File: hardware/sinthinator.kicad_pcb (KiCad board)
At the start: 2 copper layers, 100.9 x 121.4 mm, 39 parts, among them J1 3.5mm TRRS, J2 USB_C_Receptacle, SW1 SW_Push, SW2 SW_Push, SW3 SW_Push, U1 CAP1206-x-SL, U2 STM32C011J4Mx, U3 MCP4725xxx-xCH, U4 CAP1206-x-SL, U5 CAP1206-x-SL, U7 AMS1117-3.3, U8 PAM8302AAD

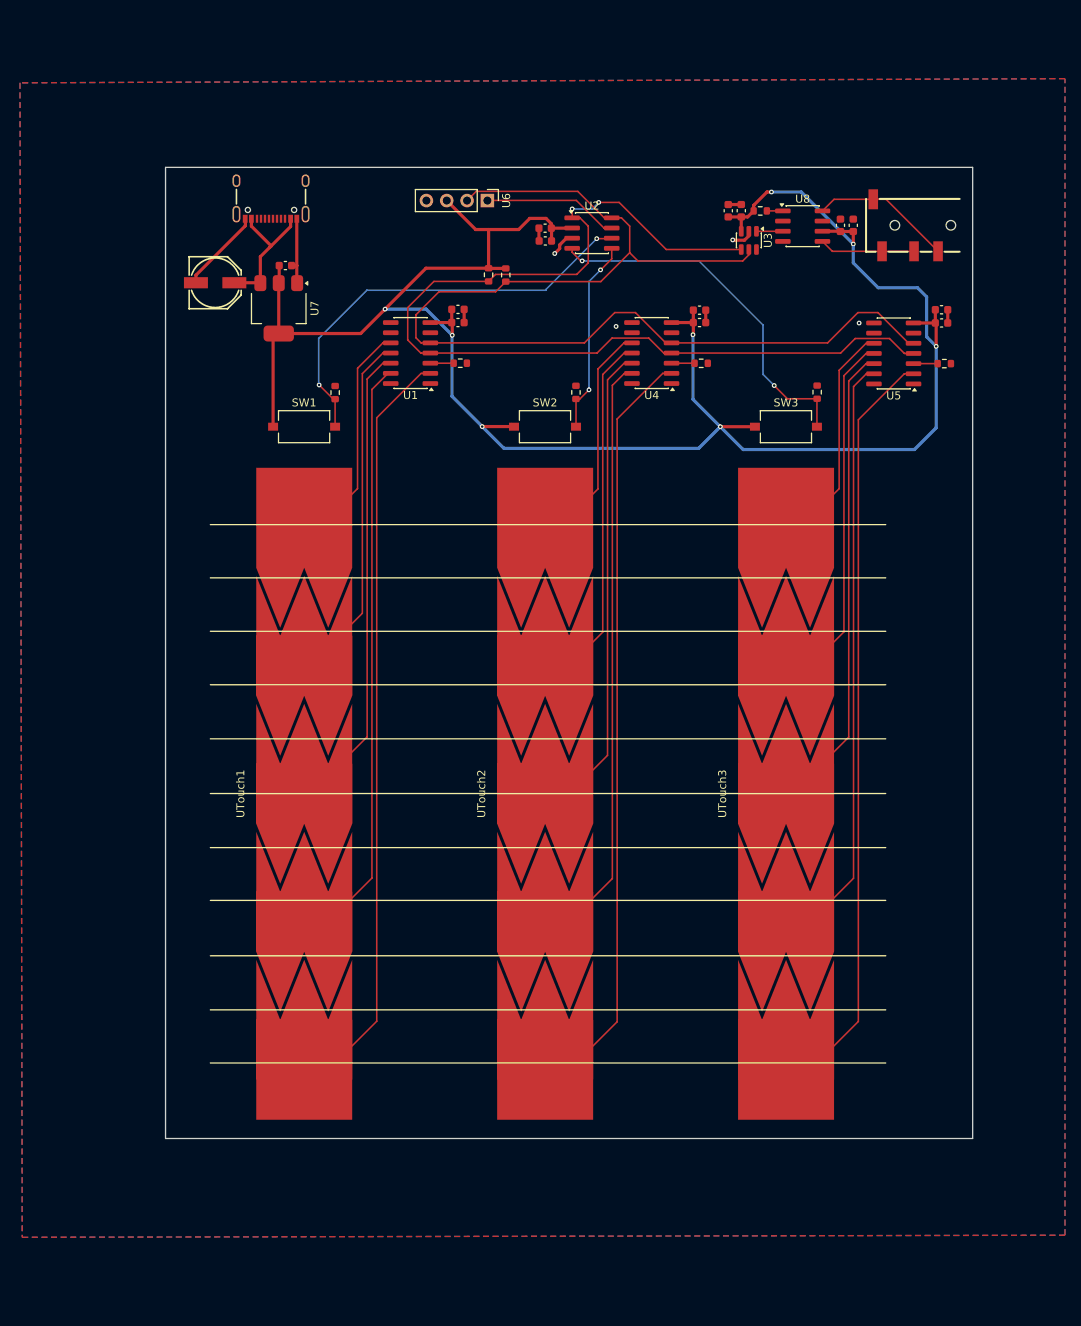
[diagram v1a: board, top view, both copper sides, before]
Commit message: Add the usb CC resistors + reduce some wasted space on board
Also added mounting holes in the same commit but don't tell anyone
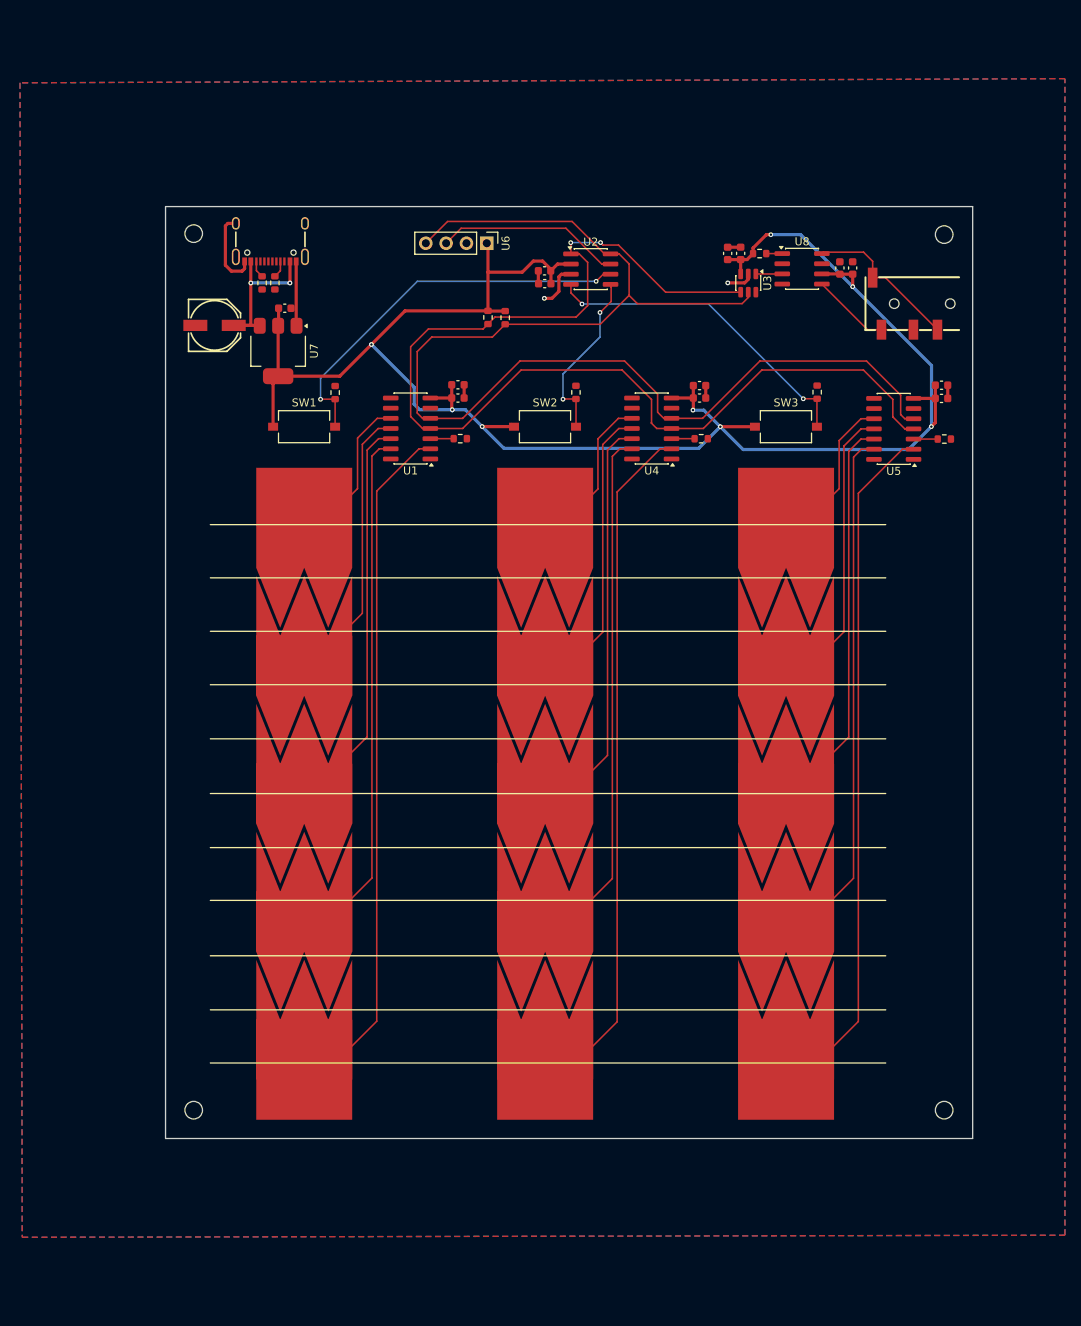
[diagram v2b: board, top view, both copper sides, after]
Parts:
- added R10: 5.1k, PCM_SparkFun-Resistor:R_0603_1608Metric, F.Cu at (113.8, 46.0)
- added R11: 5.1k, PCM_SparkFun-Resistor:R_0603_1608Metric, F.Cu at (112.2, 46.0)
- added REF**: MountingHole_2.2mm_M2, MountingHole:MountingHole_2.2mm_M2, F.Cu at (197.4, 40.0)
- added REF**: MountingHole_2.2mm_M2, MountingHole:MountingHole_2.2mm_M2, F.Cu at (103.6, 149.4)
- added REF**: MountingHole_2.2mm_M2, MountingHole:MountingHole_2.2mm_M2, F.Cu at (103.6, 39.9)
- added REF**: MountingHole_2.2mm_M2, MountingHole:MountingHole_2.2mm_M2, F.Cu at (197.4, 149.4)
- moved J1 9.79 mm to (194.7, 48.6)
- moved R8 9.43 mm to (167.1, 65.5)
- moved U1 9.43 mm to (130.7, 64.2)
- moved U4 9.43 mm to (160.9, 64.2)
- moved C10 9.43 mm to (136.7, 60.4)
- moved C11 9.43 mm to (166.9, 58.9)
- moved C12 9.43 mm to (166.9, 60.4)
- moved C13 9.43 mm to (197.1, 60.5)
- moved C14 9.43 mm to (197.1, 58.8)
- moved C9 9.43 mm to (136.7, 58.8)
- moved R7 9.43 mm to (136.9, 65.5)
- moved R9 9.43 mm to (197.4, 65.5)
- moved U5 9.43 mm to (191.1, 64.3)
- moved C1 5.33 mm to (147.5, 46.1)
- moved C2 5.33 mm to (147.5, 44.5)
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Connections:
- J2 pad A5: unconnected-(J2-CC1-PadA5) -> Net-(J2-CC1)
- J2 pad B5: unconnected-(J2-CC2-PadB5) -> Net-(J2-CC2)
- U6 pad 1: Net-(U2-PA13) -> 3.3V
- U6 pad 2: Net-(U1-SMCLK) -> GND
- U6 pad 3: 3.3V -> Net-(U2-PA13)
- U6 pad 4: GND -> Net-(U1-SMCLK)
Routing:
- net 3.3V: track 260.0 -> 232.4 mm
- net Net-(U1-SMCLK): track 143.8 -> 163.6 mm
- net Net-(U1-SMDATA): track 128.2 -> 145.0 mm
- net Net-(U5-CS1): track 93.0 -> 83.7 mm
- net Net-(U1-CS1): track 93.0 -> 83.7 mm
- net Net-(U4-CS1): track 93.0 -> 83.7 mm
- net Net-(U1-CS3): track 53.3 -> 44.1 mm
- net Net-(U4-CS2): track 72.4 -> 63.3 mm
- net Net-(U1-CS4): track 38.5 -> 29.4 mm
- net Net-(U5-CS2): track 72.4 -> 63.3 mm
- net Net-(U5-CS4): track 42.9 -> 33.9 mm
- net Net-(U5-CS5): track 25.7 -> 16.6 mm
- net Net-(U5-CS3): track 53.3 -> 44.2 mm
- net Net-(U4-CS3): track 57.6 -> 48.6 mm
- net Net-(U4-CS4): track 42.9 -> 33.9 mm
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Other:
- board size 100.9 x 121.4 mm -> 100.9 x 116.5 mm

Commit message: Update caps on power regulator
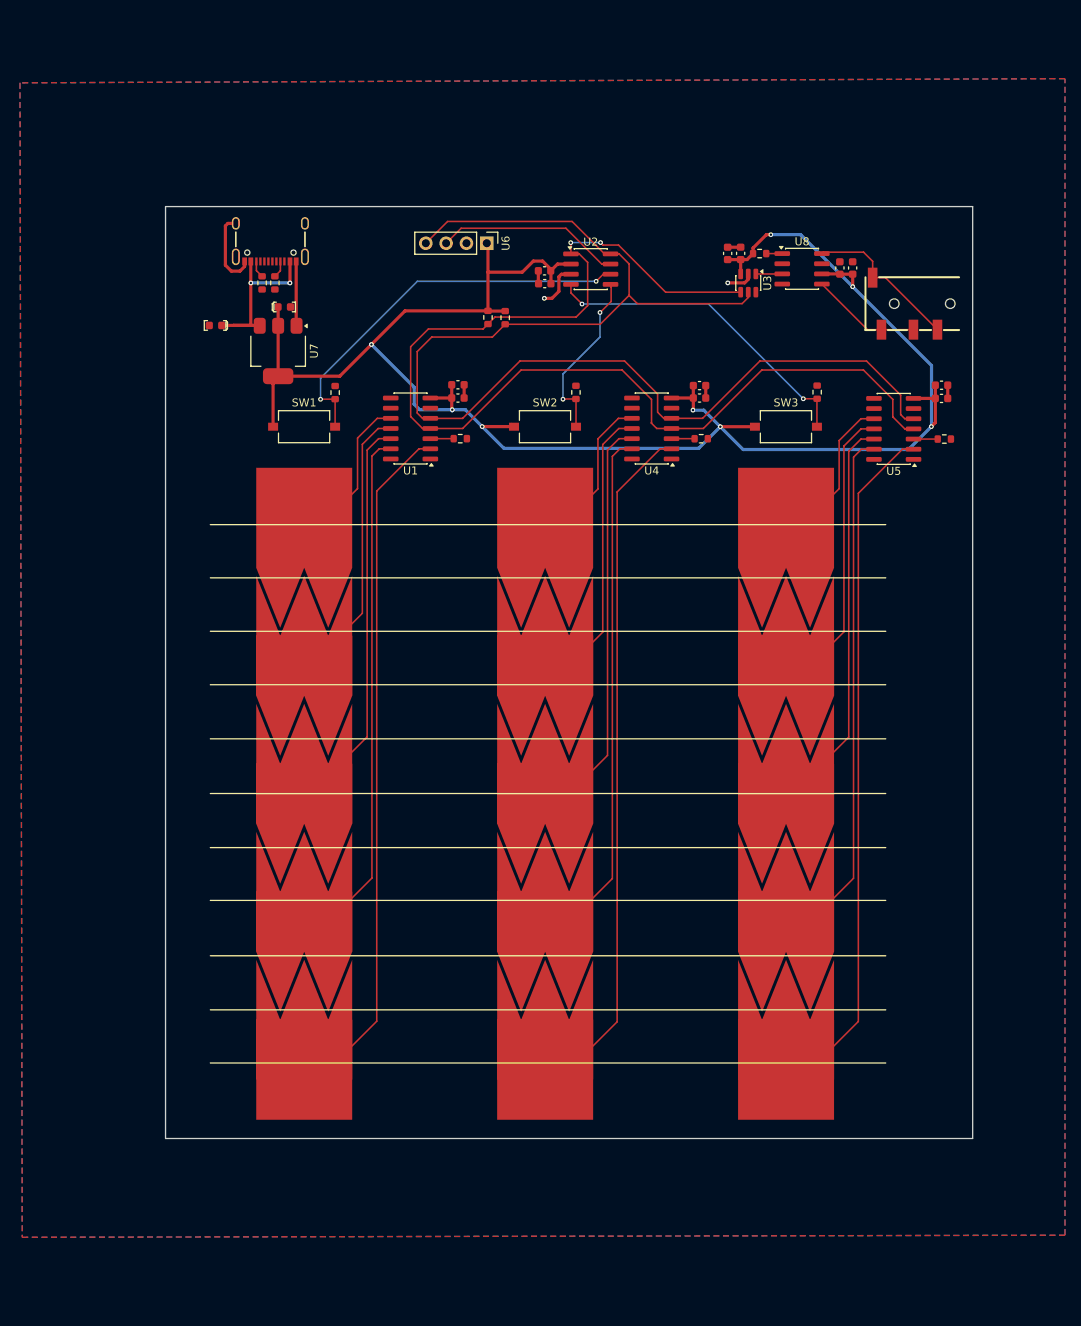
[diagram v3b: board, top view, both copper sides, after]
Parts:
- removed REF** (x4): MountingHole_2.2mm_M2, MountingHole:MountingHole_2.2mm_M2
- C3: value 22uF -> 10uF; footprint PCM_SparkFun-Capacitor:C_0603_1608Metric -> PCM_SparkFun-Capacitor:C_0603_1608Metric_Polar
- C4: value 100uF -> 10uF; footprint PCM_SparkFun-Capacitor:Panasonic_D -> PCM_SparkFun-Capacitor:C_0603_1608Metric_Polar
- moved C4 9.02 mm to (114.9, 49.0)
- moved C3 8.92 mm to (106.3, 51.4), turned to 180 degrees
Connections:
- C3 pad 1: 3.3V -> /+5V
- C4 pad 1: /+5V -> 3.3V
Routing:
- net /+5V: track 21.0 -> 22.5 mm

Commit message: Clean up + silkscreen bits
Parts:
- added M2: MountingHole_2.2mm_M2, MountingHole:MountingHole_2.2mm_M2, F.Cu at (103.8, 154.6)
- added M2: MountingHole_2.2mm_M2, MountingHole:MountingHole_2.2mm_M2, F.Cu at (197.4, 154.6)
- added M2: MountingHole_2.2mm_M2, MountingHole:MountingHole_2.2mm_M2, F.Cu at (197.4, 45.4)
- added M2: MountingHole_2.2mm_M2, MountingHole:MountingHole_2.2mm_M2, F.Cu at (103.8, 45.4)
- J2: value USB_C_Receptacle -> USB-C
- U1, U4, U5: value CAP1206-x-SL -> CAP1206
- U3: value MCP4725xxx-xCH -> MCP4725
- U8: value PAM8302AAD -> PAM8302A
- moved R5 5.24 mm to (181.6, 64.9)
- moved R9 5.24 mm to (197.4, 70.8)
- moved C11 5.24 mm to (166.9, 64.1)
- moved C14 5.24 mm to (197.1, 64.1)
- moved C3 5.24 mm to (106.3, 56.6)
- moved C4 5.24 mm to (114.9, 54.3)
- moved C5 5.24 mm to (184.4, 49.4)
- moved C6 5.24 mm to (186.0, 49.4)
- moved C7 5.24 mm to (170.4, 47.6)
- moved C8 5.24 mm to (172.0, 47.6)
- moved C9 5.24 mm to (136.7, 64.0)
- moved J1 5.24 mm to (194.7, 53.9)
- moved J2 5.24 mm to (113.2, 48.9)
- moved R1 5.24 mm to (142.6, 55.6)
- moved R10 5.24 mm to (113.8, 51.3)
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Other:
- board text added: "sinthinator v1"
- board text added: "♫"

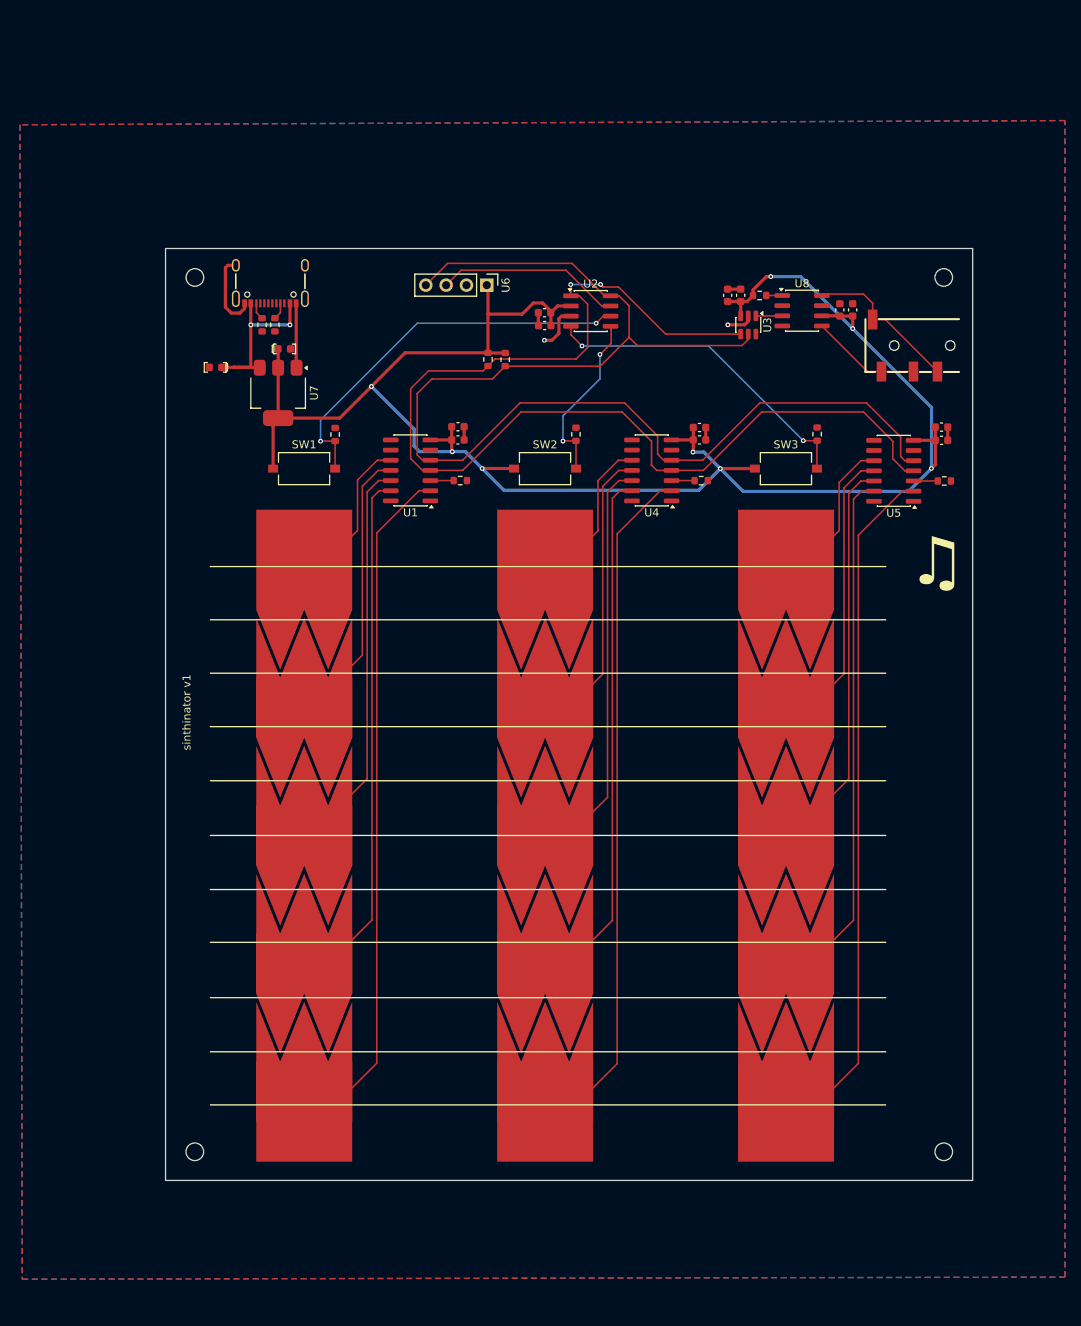
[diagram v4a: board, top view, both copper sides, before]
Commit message: Switch to STM32C011F6 for mcu to get more pins
+ add NRST header + i2s as header pins for debugging
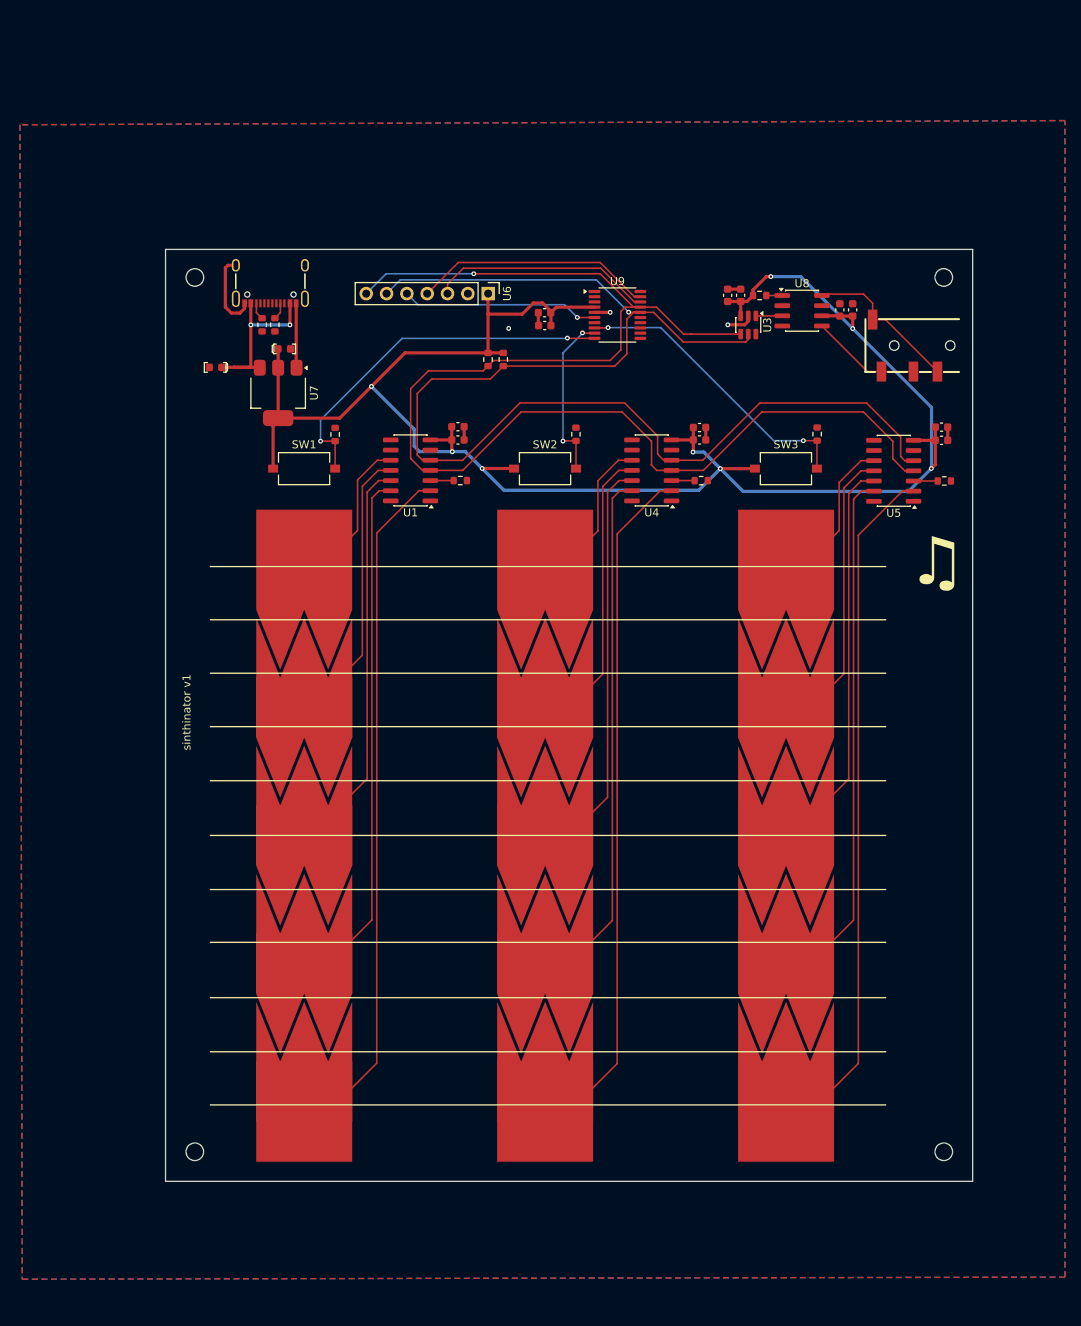
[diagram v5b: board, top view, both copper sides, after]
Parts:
- removed U2: STM32C011J4Mx, Package_SO:SOIC-8_3.9x4.9mm_P1.27mm
- added U9: STM32C011F6, Package_SO:TSSOP-20_4.4x6.5mm_P0.65mm, F.Cu at (156.6, 50.0)
- R1, R2: value 10k -> 2.2k
- U6: footprint Connector_PinHeader_2.54mm:PinHeader_1x04_P2.54mm_Vertical -> Connector_PinHeader_2.54mm:PinHeader_1x07_P2.54mm_Vertical
- moved U6 1.07 mm to (140.4, 47.4)
- moved R1 0.24 mm to (142.3, 55.6), turned to -90 degrees
- turned R2 to -90 degrees
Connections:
- R1 pad 1: Net-(U1-SMCLK) -> 3.3V
- R1 pad 2: 3.3V -> I2C_SCK
- R2 pad 1: Net-(U1-SMDATA) -> 3.3V
- R2 pad 2: 3.3V -> I2C_SDA
- U1 pad 4: Net-(U1-SMDATA) -> I2C_SDA
- U1 pad 5: Net-(U1-SMCLK) -> I2C_SCK
- U3 pad 4: Net-(U1-SMDATA) -> I2C_SDA
- U3 pad 5: Net-(U1-SMCLK) -> I2C_SCK
- U4 pad 4: Net-(U1-SMDATA) -> I2C_SDA
- U4 pad 5: Net-(U1-SMCLK) -> I2C_SCK
- U5 pad 4: Net-(U1-SMDATA) -> I2C_SDA
- U5 pad 5: Net-(U1-SMCLK) -> I2C_SCK
- U6 pad 3: Net-(U2-PA13) -> SWDIO
- U6 pad 4: Net-(U1-SMCLK) -> SWDCLK
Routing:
- net I2C_SDA: track 0.00 -> 174.1 mm, vias 0 -> 1
- net I2C_SCK: track 0.00 -> 169.8 mm, vias 0 -> 1
- net Net-(U1-SMCLK): track 163.6 -> 0.00 mm
- net Net-(U1-SMDATA): track 145.0 -> 0.00 mm, vias 2 -> 0
- net SWDCLK: track 0.00 -> 30.0 mm
- net SWDIO: track 0.00 -> 27.9 mm
- net NRST: track 0.00 -> 24.7 mm, vias 0 -> 1
- net Net-(U2-PA13): track 23.2 -> 0.00 mm
- net GND: track 35.5 -> 31.8 mm, vias 2 -> 3
- net Net-(U9-PA1): track 40.8 -> 37.2 mm
- net Net-(U9-PA3): track 49.5 -> 46.4 mm
- net 3.3V: track 232.6 -> 234.2 mm
- net Net-(U9-PA2): track 22.0 -> 21.2 mm
